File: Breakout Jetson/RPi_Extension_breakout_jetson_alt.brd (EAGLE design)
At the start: 63 x 70.1 mm, 24 parts, among them U1 Value, U10 74AHC1G04GW/T1, U11 74AHC1G04GW/T1, U12 74AHC1G04GW/T1, U13 74AHC1G04GW/T1, U14 74AHC1G04GW/T1, U15 74AHC1G04GW/T1, U16 74AHC1G04GW/T1, U17 74AHC1G04GW/T1, U2 74AHC1G04GW/T1, U3 74AHC1G04GW/T1, U4 74AHC1G04GW/T1, U5 74AHC1G04GW/T1, U6 74AHC1G04GW/T1, U7 74AHC1G04GW/T1, U8 74AHC1G04GW/T1, U9 74AHC1G04GW/T1

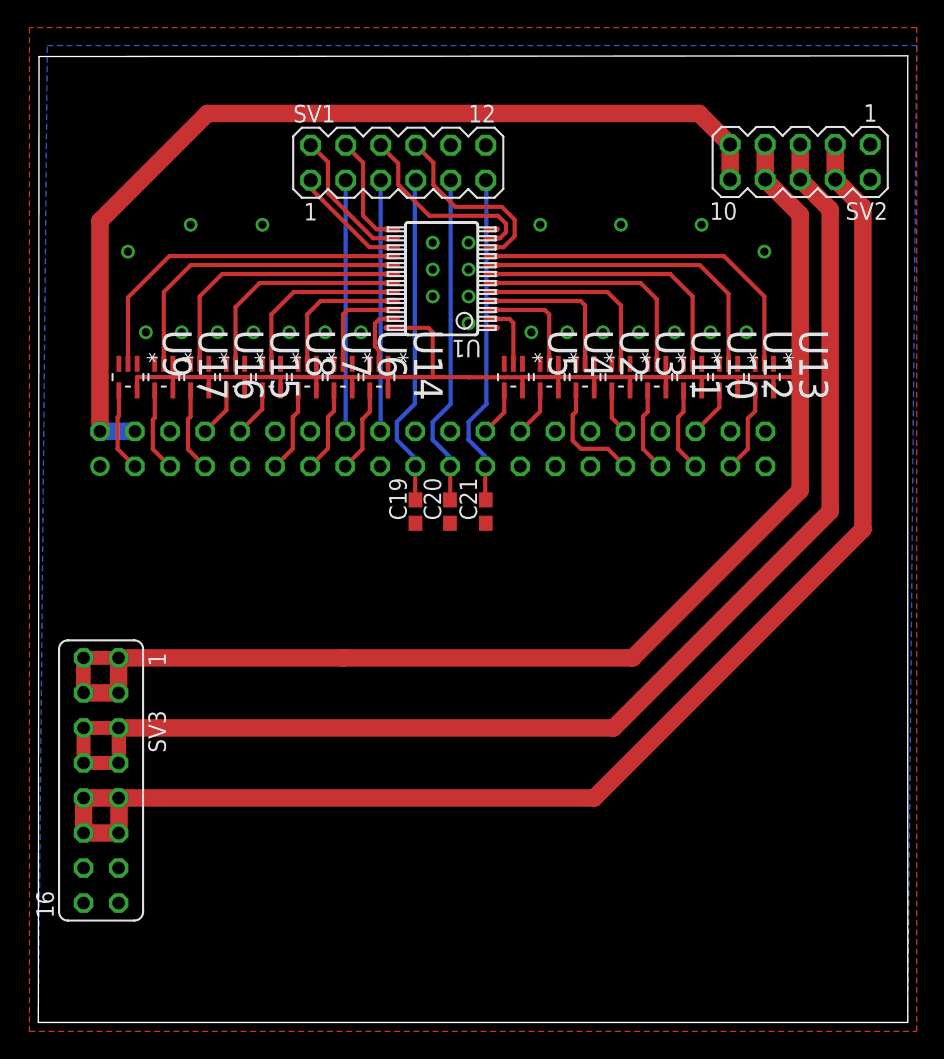
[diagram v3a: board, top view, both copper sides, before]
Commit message: made pads of multiplexer square and started to solve remaining drc errors
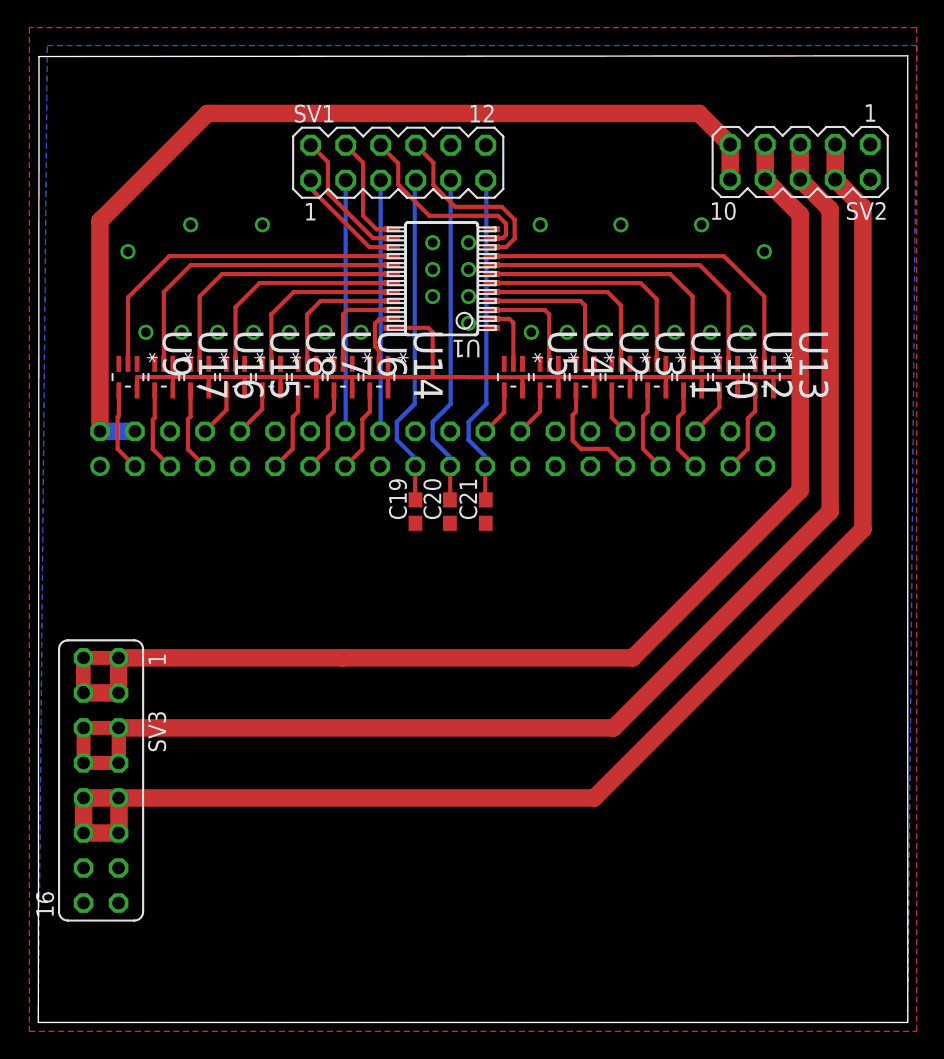
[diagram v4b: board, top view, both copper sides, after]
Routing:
- net DVCC: vias 3 -> 2
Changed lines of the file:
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@@
 <contactref element="SV5" pad="34"/>
 <contactref element="SV5" pad="39"/>
-<contactref element="U1" pad="12"/>
 <contactref element="U5" pad="3"/>
 <contactref element="U4" pad="3"/>
@@
 <contactref element="U16" pad="3"/>
 <contactref element="U17" pad="3"/>
-<via x="7.8" y="50.05" extent="1-16" drill="0.6"/>
-<via x="10.4" y="50.05" extent="1-16" drill="0.6"/>
-<via x="13" y="50.05" extent="1-16" drill="0.6"/>
-<via x="15.6" y="50.05" extent="1-16" drill="0.6"/>
-<via x="18.2" y="50.05" extent="1-16" drill="0.6"/>
-<via x="20.8" y="50.05" extent="1-16" drill="0.6"/>
-<via x="35.75" y="50.05" extent="1-16" drill="0.6"/>
-<via x="38.35" y="50.05" extent="1-16" drill="0.6"/>
-<via x="40.95" y="50.05" extent="1-16" drill="0.6"/>
-<via x="43.55" y="50.05" extent="1-16" drill="0.6"/>
-<via x="46.15" y="50.05" extent="1-16" drill="0.6"/>
-<via x="48.75" y="50.05" extent="1-16" drill="0.6"/>
-<via x="51.35" y="50.05" extent="1-16" drill="0.6"/>
-<via x="23.4" y="50.05" extent="1-16" drill="0.6"/>
-<via x="28.6" y="52.65" extent="1-16" drill="0.6"/>
-<via x="28.6" y="54.6" extent="1-16" drill="0.6"/>
-<via x="28.6" y="56.55" extent="1-16" drill="0.6"/>
-<via x="31.2" y="50.7" extent="1-16" drill="0.6"/>
-<via x="6.5" y="55.9" extent="1-16" drill="0.6"/>
-<via x="52.65" y="55.9" extent="1-16" drill="0.6"/>
-<via x="16.25" y="57.85" extent="1-16" drill="0.6"/>
-<via x="36.4" y="57.85" extent="1-16" drill="0.6"/>
-<via x="42.25" y="57.85" extent="1-16" drill="0.6"/>
-<via x="11.05" y="57.85" extent="1-16" drill="0.6"/>
-<via x="48.1" y="57.85" extent="1-16" drill="0.6"/>
-<via x="31.2" y="56.55" extent="1-16" drill="0.6"/>
-<via x="31.2" y="54.6" extent="1-16" drill="0.6"/>
-<via x="31.2" y="52.65" extent="1-16" drill="0.6"/>
+<via x="7.8" y="50.05" extent="1-16" drill="0.7"/>
+<via x="10.4" y="50.05" extent="1-16" drill="0.7"/>
+<via x="13" y="50.05" extent="1-16" drill="0.7"/>
+<via x="15.6" y="50.05" extent="1-16" drill="0.7"/>
+<via x="18.2" y="50.05" extent="1-16" drill="0.7"/>
+<via x="20.8" y="50.05" extent="1-16" drill="0.7"/>
+<via x="35.75" y="50.05" extent="1-16" drill="0.7"/>
+<via x="38.35" y="50.05" extent="1-16" drill="0.7"/>
+<via x="40.95" y="50.05" extent="1-16" drill="0.7"/>
+<via x="43.55" y="50.05" extent="1-16" drill="0.7"/>
+<via x="46.15" y="50.05" extent="1-16" drill="0.7"/>
+<via x="48.75" y="50.05" extent="1-16" drill="0.7"/>
+<via x="51.35" y="50.05" extent="1-16" drill="0.7"/>
+<via x="23.4" y="50.05" extent="1-16" drill="0.7"/>
+<via x="28.6" y="52.65" extent="1-16" drill="0.7"/>
+<via x="28.6" y="54.6" extent="1-16" drill="0.7"/>
+<via x="28.6" y="56.55" extent="1-16" drill="0.7"/>
+<via x="31.2" y="50.7" extent="1-16" drill="0.7"/>
+<via x="6.5" y="55.9" extent="1-16" drill="0.7"/>
+<via x="52.65" y="55.9" extent="1-16" drill="0.7"/>
+<via x="16.25" y="57.85" extent="1-16" drill="0.7"/>
+<via x="36.4" y="57.85" extent="1-16" drill="0.7"/>
+<via x="42.25" y="57.85" extent="1-16" drill="0.7"/>
+<via x="11.05" y="57.85" extent="1-16" drill="0.7"/>
+<via x="48.1" y="57.85" extent="1-16" drill="0.7"/>
+<via x="31.2" y="56.55" extent="1-16" drill="0.7"/>
+<via x="31.2" y="54.6" extent="1-16" drill="0.7"/>
+<via x="31.2" y="52.65" extent="1-16" drill="0.7"/>
+<contactref element="U1" pad="12"/>
 </signal>
 <signal name="DVCC">
@@
 <wire x1="28.6" y1="26.79" x2="22.2" y2="26.54" width="0.3048" layer="1"/>
 <wire x1="22.2" y1="26.54" x2="22.1" y2="26.44" width="0.3048" layer="1"/>
-<via x="3.25" y="26.44" extent="1-16" drill="0.7"/>
 <via x="3.25" y="24.05" extent="1-16" drill="0.7"/>
 <via x="3.28" y="24.05" extent="1-16" drill="0.7"/>
@@
 <wire x1="26.1" y1="62.3" x2="26.1" y2="60.75886875" width="0.3048" layer="1"/>
 <wire x1="26.1" y1="60.75886875" x2="28.35886875" y2="58.5" width="0.3048" layer="1"/>
-<wire x1="33.475" y1="56.875" x2="33.91106875" y2="57.31106875" width="0.3048" layer="1"/>
-<wire x1="33.91106875" y1="57.31106875" x2="33.91106875" y2="57.92795625" width="0.3048" layer="1"/>
+<wire x1="32.875" y1="56.875" x2="33.67793125" y2="56.875" width="0.3048" layer="1"/>
+<wire x1="33.67793125" y1="56.875" x2="33.91106875" y2="57.1081375" width="0.3048" layer="1"/>
+<wire x1="33.91106875" y1="57.1081375" x2="33.91106875" y2="57.92795625" width="0.3048" layer="1"/>
 <wire x1="33.91106875" y1="57.92795625" x2="33.339025" y2="58.5" width="0.3048" layer="1"/>
 <wire x1="33.339025" y1="58.5" x2="28.35886875" y2="58.5" width="0.3048" layer="1"/>
-<wire x1="32.875" y1="56.875" x2="33.475" y2="56.875" width="0.3048" layer="1"/>
 </signal>
 <signal name="EN_MULT">
@@
 <wire x1="27.37" y1="63.62" x2="27.38" y2="63.62" width="0.3048" layer="1"/>
 <wire x1="27.38" y1="63.62" x2="28.65" y2="62.35" width="0.3048" layer="1"/>
-<wire x1="33.742453125" y1="56.225003125" x2="34.5437375" y2="57.0262875" width="0.3048" layer="1"/>
-<wire x1="34.5437375" y1="57.0262875" x2="34.5437375" y2="58.2181125" width="0.3048" layer="1"/>
+<wire x1="32.875" y1="56.225003125" x2="33.916221875" y2="56.225003125" width="0.3048" layer="1"/>
+<wire x1="33.916221875" y1="56.225003125" x2="34.5437375" y2="56.85251875" width="0.3048" layer="1"/>
+<wire x1="34.5437375" y1="56.85251875" x2="34.5437375" y2="58.2181125" width="0.3048" layer="1"/>
 <wire x1="34.5437375" y1="58.2181125" x2="33.61185" y2="59.15" width="0.3048" layer="1"/>
 <wire x1="33.61185" y1="59.15" x2="30.2311375" y2="59.15" width="0.3048" layer="1"/>
 <wire x1="30.2311375" y1="59.15" x2="28.65" y2="60.7311375" width="0.3048" layer="1"/>
 <wire x1="28.65" y1="60.7311375" x2="28.65" y2="62.35" width="0.3048" layer="1"/>
-<wire x1="32.875" y1="56.225003125" x2="33.742453125" y2="56.225003125" width="0.3048" layer="1"/>
 </signal>
 <signal name="ADDR4">
